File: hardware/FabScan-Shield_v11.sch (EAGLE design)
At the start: 44 parts, among them T1A BC547, T1B IRLML2502, X1 PASSER, X2 PASSER, X3 PASSER

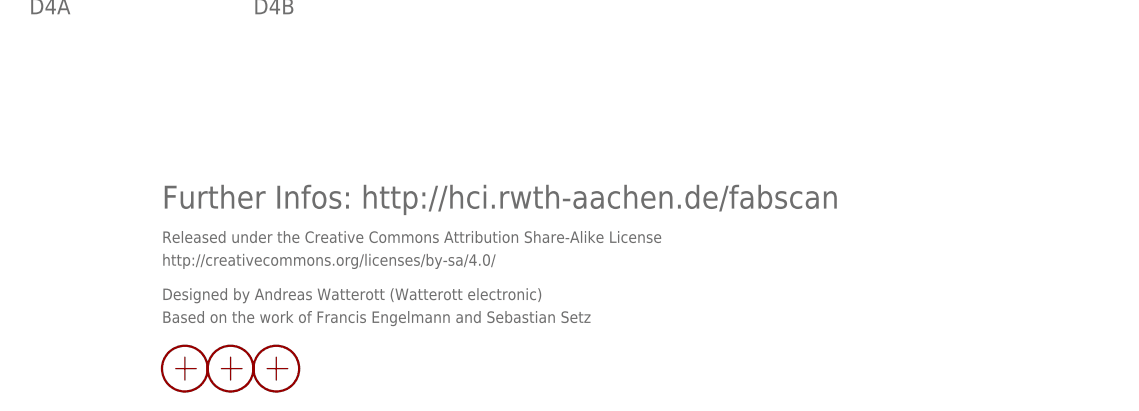
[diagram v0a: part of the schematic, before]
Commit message: updated schematics
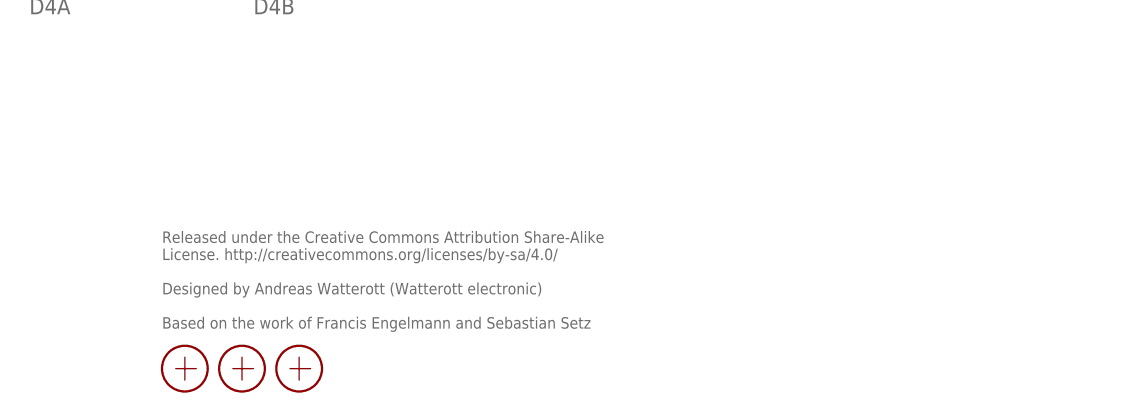
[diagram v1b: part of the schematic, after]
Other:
- note added: "Released under the Creative Commons Attribution Share-Alike License. http://creativecommons.org/licenses/by-sa/4.0/ Designed by Andreas Watterott (Watterott electronic) Based on the work of Francis Engelmann and Sebastian Setz"
- note removed: "Based on the work of Francis Engelmann and Sebastian Setz"
- note removed: "Designed by Andreas Watterott (Watterott electronic)"
- note removed: "Further Infos: http://hci.rwth-aachen.de/fabscan"
- note removed: "Released under the Creative Commons Attribution Share-Alike License"
- note removed: "http://creativecommons.org/licenses/by-sa/4.0/"
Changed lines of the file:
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@@
 <?xml version="1.0" encoding="utf-8"?>
 <!DOCTYPE eagle SYSTEM "eagle.dtd">
-<eagle version="6.6.0">
+<eagle version="7.5.0">
 <drawing>
 <settings>
@@
 <setting verticaltext="up"/>
 </settings>
-<grid distance="0.05" unitdist="inch" unit="inch" style="lines" multiple="1" display="yes" altdistance="0.025" altunitdist="inch" altunit="inch"/>
+<grid distance="0.1" unitdist="inch" unit="inch" style="lines" multiple="1" display="no" altdistance="0.01" altunitdist="inch" altunit="inch"/>
 <layers>
 <layer number="1" name="Top" color="4" fill="1" visible="no" active="no"/>
@@
 <layer number="51" name="tDocu" color="7" fill="1" visible="no" active="no"/>
 <layer number="52" name="bDocu" color="7" fill="1" visible="no" active="no"/>
-<layer number="53" name="tCopper" color="7" fill="11" visible="no" active="no"/>
-<layer number="54" name="bCopper" color="7" fill="1" visible="no" active="no"/>
-<layer number="56" name="wert" color="7" fill="1" visible="no" active="no"/>
 <layer number="91" name="Nets" color="2" fill="1" visible="yes" active="yes"/>
 <layer number="92" name="Busses" color="1" fill="1" visible="yes" active="yes"/>
@@
 <layer number="97" name="Info" color="7" fill="1" visible="yes" active="yes"/>
 <layer number="98" name="Guide" color="6" fill="1" visible="yes" active="yes"/>
-<layer number="100" name="Muster" color="7" fill="1" visible="no" active="no"/>
-<layer number="251" name="SMDround" color="12" fill="11" visible="no" active="no"/>
 </layers>
 <schematic xreflabel="%F%N/%S.%C%R" xrefpart="/%S.%C%R">
@@
 <plain>
 <wire x1="33.02" y1="157.48" x2="35.687" y2="157.48" width="0.8128" layer="94"/>
-<text x="162.56" y="21.59" size="1.27" layer="95">Released under the Creative Commons Attribution Share-Alike License</text>
-<text x="162.56" y="19.05" size="1.27" layer="95">http://creativecommons.org/licenses/by-sa/4.0/</text>
-<text x="162.56" y="15.24" size="1.27" layer="95">Designed by Andreas Watterott (Watterott electronic)</text>
-<text x="162.56" y="25.4" size="2.54" layer="95">Further Infos: http://hci.rwth-aachen.de/fabscan</text>
-<text x="162.56" y="12.7" size="1.27" layer="95">Based on the work of Francis Engelmann and Sebastian Setz</text>
+<text x="162.56" y="22.86" size="1.27" layer="95" align="top-left">Released under the Creative Commons Attribution Share-Alike
+License. http://creativecommons.org/licenses/by-sa/4.0/
+Designed by Andreas Watterott (Watterott electronic)
+Based on the work of Francis Engelmann and Sebastian Setz</text>
 <text x="209.55" y="166.37" size="2.54" layer="95">Servos</text>
 <text x="189.23" y="166.37" size="2.54" layer="95">Steppers</text>
@@
 </instance>
 <instance part="X1" gate="G$1" x="165.1" y="7.62" smashed="yes"/>
-<instance part="X2" gate="G$1" x="170.18" y="7.62" smashed="yes"/>
+<instance part="X2" gate="G$1" x="171.45" y="7.62" smashed="yes"/>
 <instance part="D1" gate="G$1" x="157.48" y="142.24" rot="R180"/>
 <instance part="R1" gate="G$1" x="157.48" y="152.4" smashed="yes" rot="R270">
@@
 <attribute name="VALUE" x="224.79" y="64.77" size="1.778" layer="96" rot="MR270"/>
 </instance>
-<instance part="X3" gate="G$1" x="175.26" y="7.62" smashed="yes"/>
+<instance part="X3" gate="G$1" x="177.8" y="7.62" smashed="yes"/>
 <instance part="FRAME1" gate="G$1" x="0" y="0"/>
 </instances>
@@
 </schematic>
 </drawing>
+<compatibility>
+<note version="6.3" minversion="6.2.2" severity="warning">
+Since Version 6.2.2 text objects can contain more than one line,
+which will not be processed correctly with this version.
+</note>
+</compatibility>
 </eagle>
